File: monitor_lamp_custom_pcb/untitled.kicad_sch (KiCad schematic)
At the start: 14 parts, among them J10 Conn_01x01, J2 VEML7700_Connection, J3 LD2410C_Connection, J4 Conn_01x02, J5 SHTxx_Connection, J7 Conn_01x01, J8 Conn_01x01, J9 Conn_01x01, Q2 AO3401A, Q3 AO3400A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

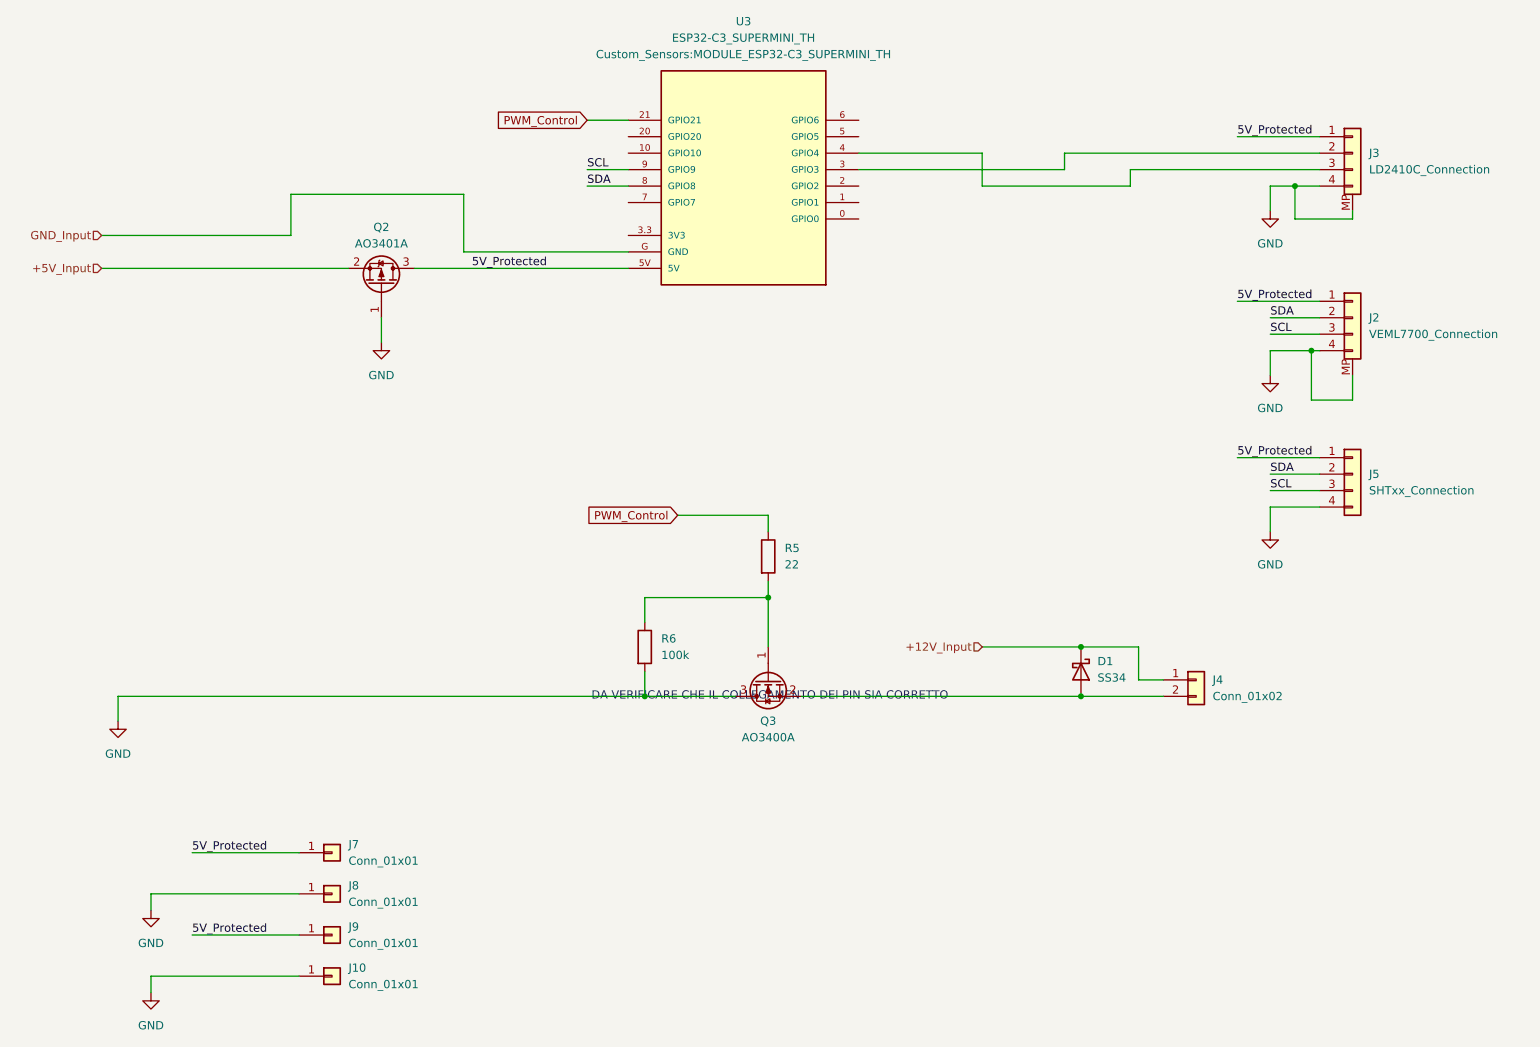
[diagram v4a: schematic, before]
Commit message: Remodelled the scheme with 12V input
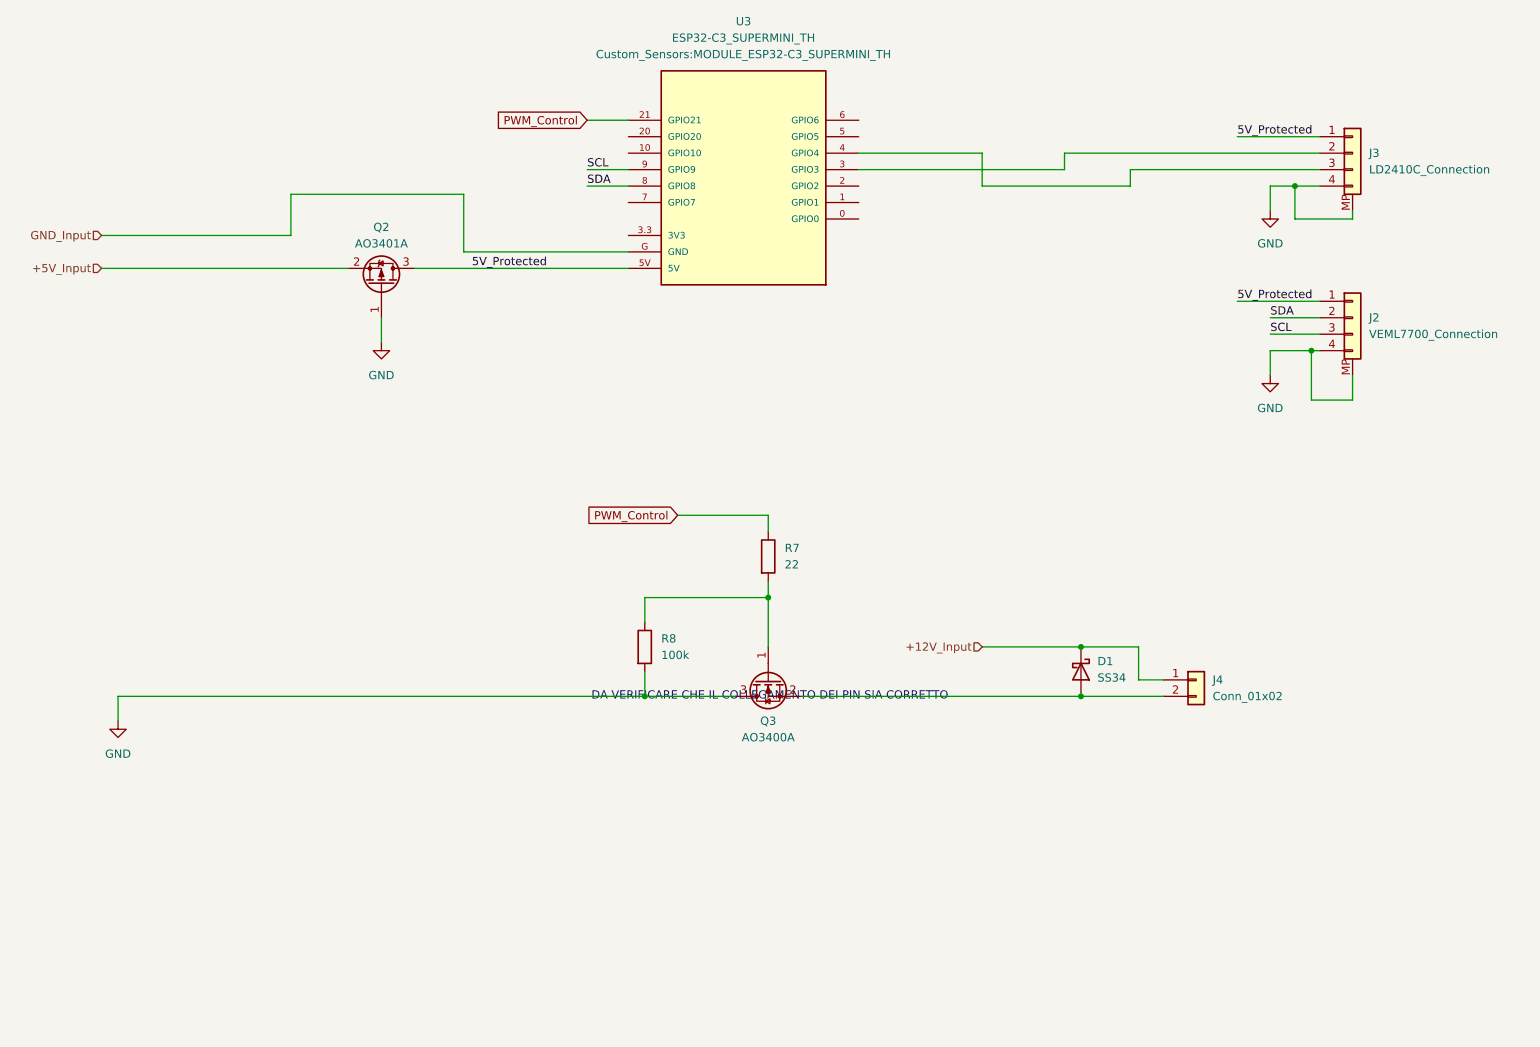
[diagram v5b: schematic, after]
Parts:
- removed J10, J7, J8, J9: Conn_01x01, TestPoint:TestPoint_Pad_1.0x1.0mm, symbol Connector_Generic:Conn_01x01
- removed J5: SHTxx_Connection, Connector_PinHeader_2.54mm:PinHeader_1x04_P2.54mm_Vertical, symbol Connector_Generic:Conn_01x04
- renumbered R5 to R7, R6 to R8

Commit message: Placed connection pad
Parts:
- added J8, J9: Conn_01x01, Connector_Wire:SolderWirePad_1x01_SMD_2x4mm, symbol Connector_Generic:Conn_01x01
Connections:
- net 5V_Protected: now also J8.1 (Pin_1)
- net GND: now also J9.1 (Pin_1)

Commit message: Terminated design, generated fabrication files for JLCPCB
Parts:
- J2, J3, J4, U3: now left out of the parts list
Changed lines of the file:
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@@
 		(body_style 1)
 		(exclude_from_sim no)
-		(in_bom yes)
+		(in_bom no)
 		(on_board yes)
 		(in_pos_files yes)
@@
 		(body_style 1)
 		(exclude_from_sim no)
-		(in_bom yes)
+		(in_bom no)
 		(on_board yes)
 		(in_pos_files yes)
@@
 		(body_style 1)
 		(exclude_from_sim no)
-		(in_bom yes)
+		(in_bom no)
 		(on_board yes)
 		(in_pos_files yes)
@@
 		(body_style 1)
 		(exclude_from_sim no)
-		(in_bom yes)
+		(in_bom no)
 		(on_board yes)
 		(in_pos_files yes)

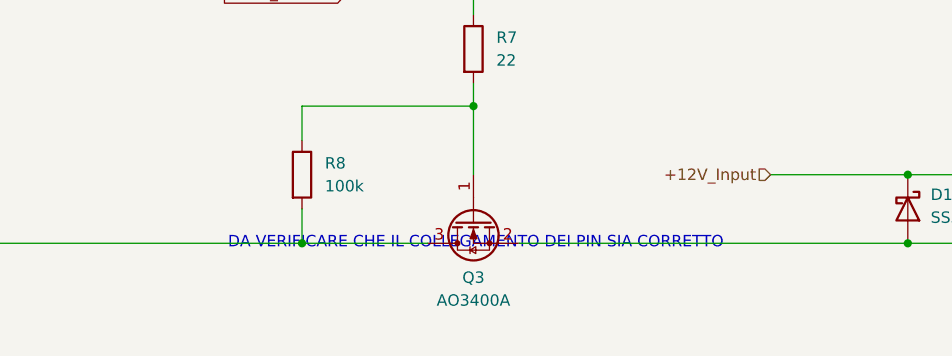
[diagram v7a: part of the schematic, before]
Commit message: Added some drawing to the board and recreated fabbrication file
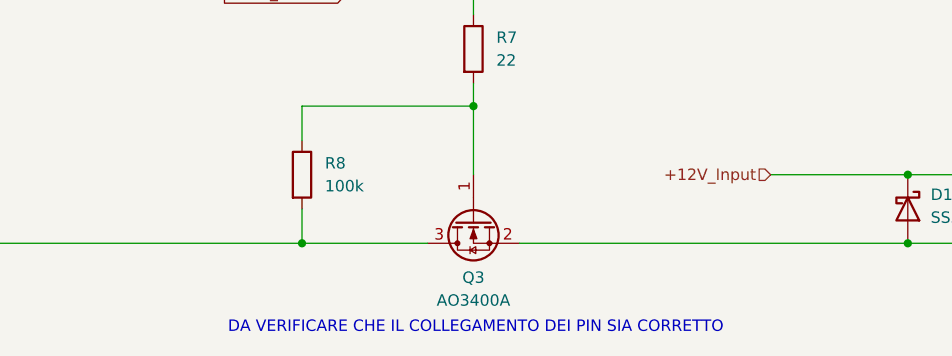
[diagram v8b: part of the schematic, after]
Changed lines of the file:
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@@
 	(text "DA VERIFICARE CHE IL COLLEGAMENTO DEI PIN SIA CORRETTO\n"
 		(exclude_from_sim no)
-		(at 143.764 132.08 0)
+		(at 143.764 141.478 0)
 		(effects
 			(font
